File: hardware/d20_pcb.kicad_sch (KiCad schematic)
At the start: 37 parts, among them J1 Conn_01x06_Socket, J2 Conn_01x01_Pin, SW1 SW_SPST, SW2 SW_Push, U1 ATtiny84-20P

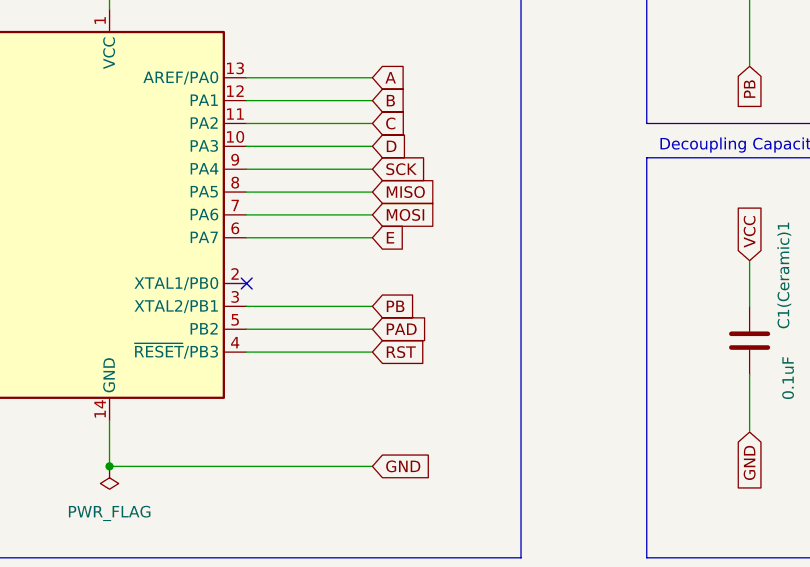
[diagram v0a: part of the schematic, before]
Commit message: HW: Add d20v3
Changes:
- move touchpad to analog pin
- resize map artwork
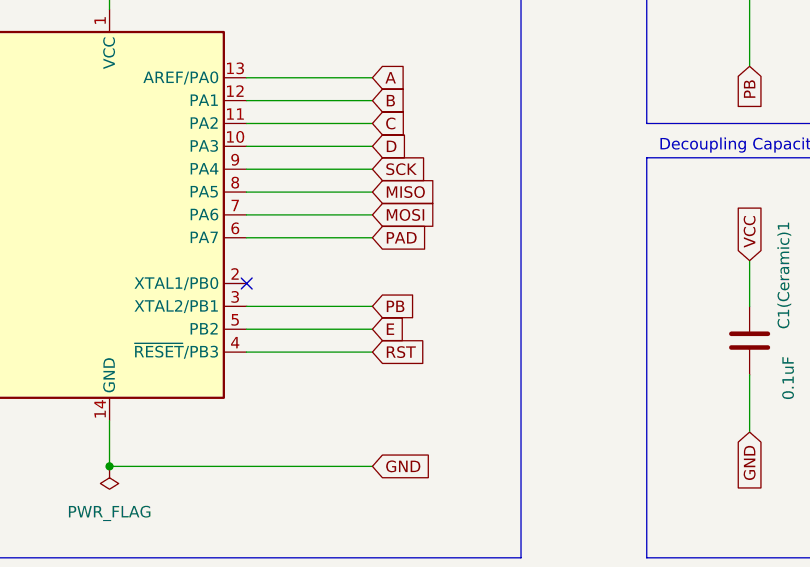
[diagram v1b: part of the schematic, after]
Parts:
- U1: footprint Package_DIP:DIP-14_W7.62mm -> Package_SO:SOIC-14_3.9x8.7mm_P1.27mm
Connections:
- net E: now also U1.5 (PB2); no longer U1.6 (PA7)
- net PAD: now also U1.6 (PA7); no longer U1.5 (PB2)
